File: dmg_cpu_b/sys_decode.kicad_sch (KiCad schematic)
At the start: 94 parts, among them T1 IBUF, T2 IBUF

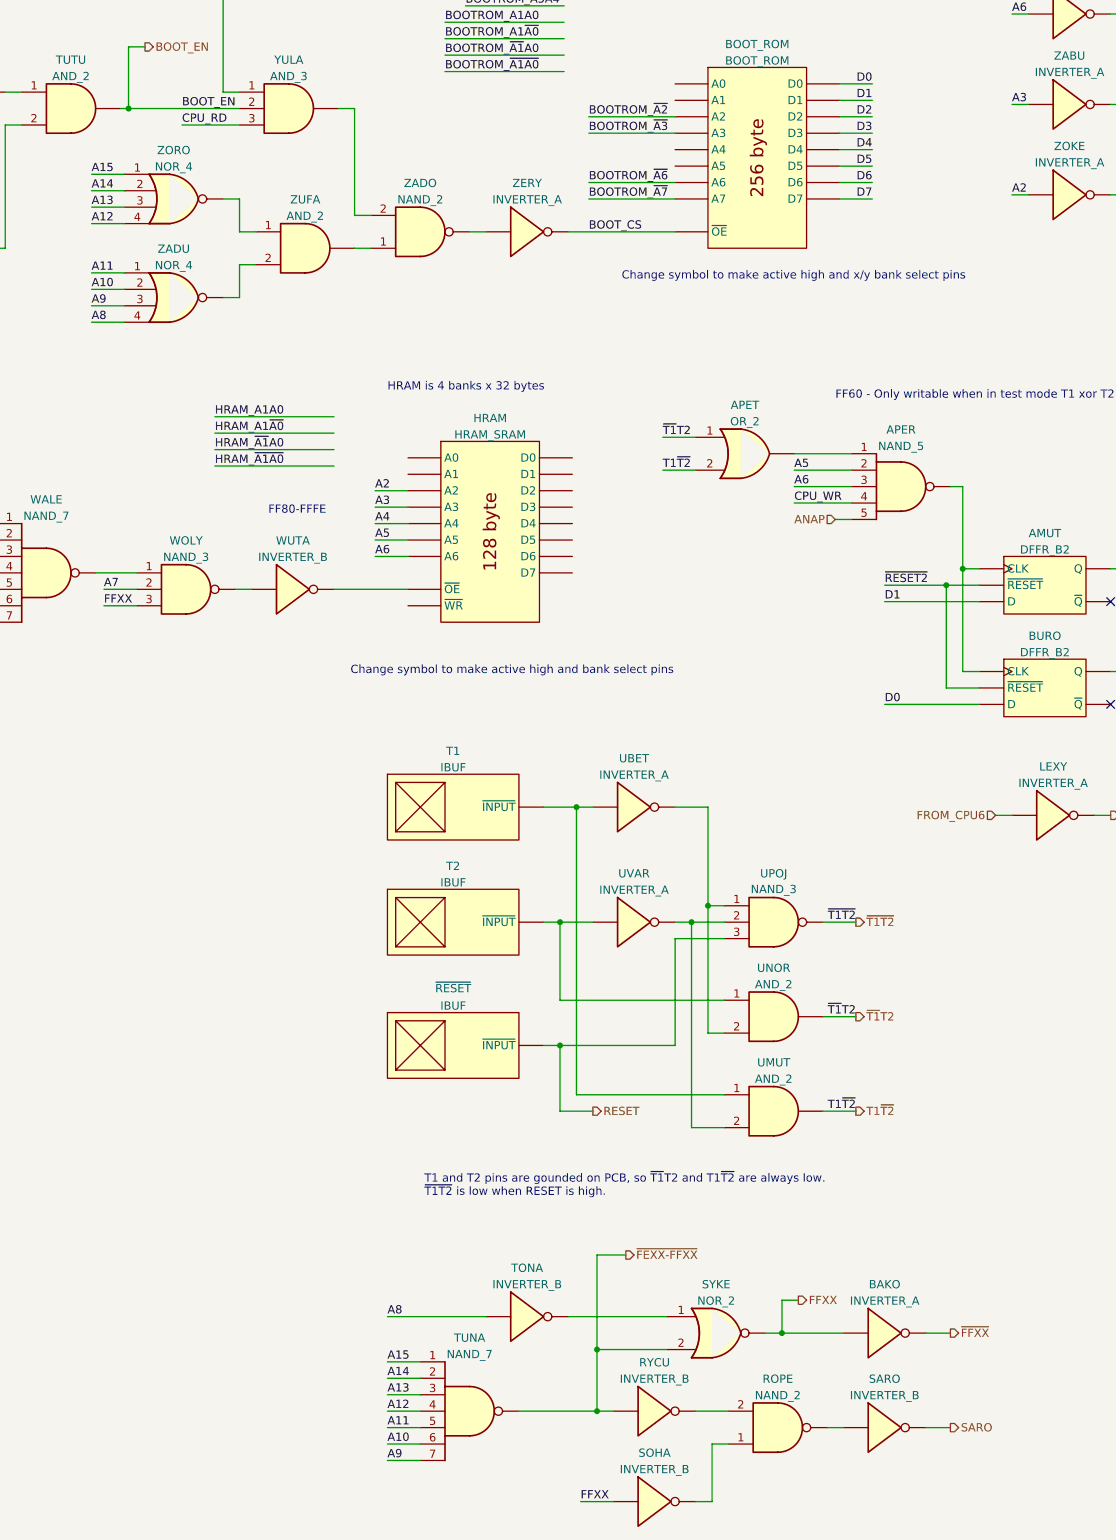
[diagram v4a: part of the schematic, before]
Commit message: Fixes made from issues, channel 4 sheet aded and tidy up of hierarchical APU sheet. Small fixes done here and there when doing ERC.
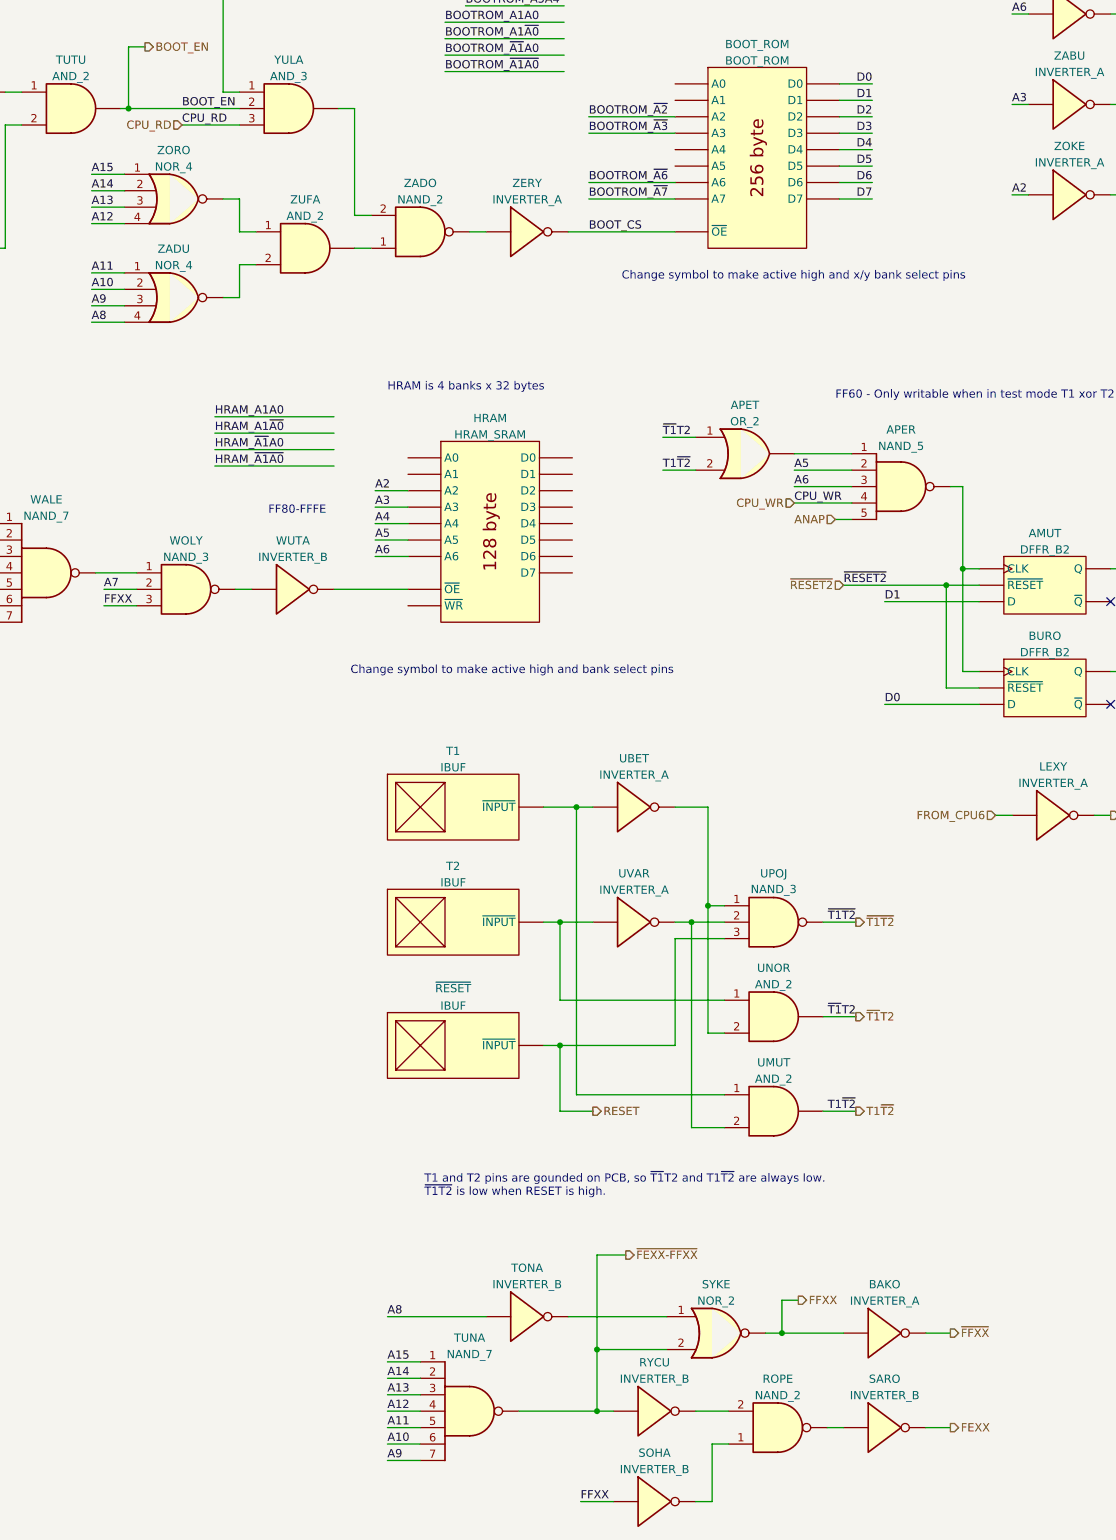
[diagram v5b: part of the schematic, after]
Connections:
- net SARO renamed FEXX
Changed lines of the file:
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@@
     (stroke (width 0) (type default) (color 0 0 0 0))
   )
-  (wire (pts (xy 271.145 132.08) (xy 280.67 132.08))
+  (wire (pts (xy 264.795 132.08) (xy 280.67 132.08))
     (stroke (width 0) (type default) (color 0 0 0 0))
   )
@@
     (effects (font (size 1.27 1.27)) (justify left bottom))
   )
-  (label "~{RESET2}" (at 271.145 132.08 0)
+  (label "~{RESET2}" (at 264.795 132.08 0)
     (effects (font (size 1.27 1.27)) (justify left bottom))
   )
@@
     (effects (font (size 1.27 1.27)) (justify left))
   )
+  (hierarchical_label "CPU_RD" (shape input) (at 162.56 60.96 180)
+    (effects (font (size 1.27 1.27)) (justify right))
+  )
+  (hierarchical_label "CPU_WR" (shape input) (at 257.175 119.38 180)
+    (effects (font (size 1.27 1.27)) (justify right))
+  )
   (hierarchical_label "FROM_CPU6" (shape input) (at 288.29 167.64 180)
     (effects (font (size 1.27 1.27)) (justify right))
@@
     (effects (font (size 1.27 1.27)) (justify left))
   )
+  (hierarchical_label "~{RESET2}" (shape input) (at 264.795 132.08 180)
+    (effects (font (size 1.27 1.27)) (justify right))
+  )
   (hierarchical_label "FF60_D0" (shape output) (at 308.61 145.415 0)
     (effects (font (size 1.27 1.27)) (justify left))
@@
     (effects (font (size 1.27 1.27)) (justify left))
   )
-  (hierarchical_label "SARO" (shape output) (at 281.305 262.255 0)
+  (hierarchical_label "FEXX" (shape output) (at 281.305 262.255 0)
     (effects (font (size 1.27 1.27)) (justify left))
   )
@@
   (symbol (lib_id "power:GND") (at 90.17 269.24 0) (unit 1)
     (in_bom yes) (on_board yes) (fields_autoplaced)
-    (property "Reference" "#PWR?" (id 0) (at 90.17 275.59 0)
+    (property "Reference" "#PWR0107" (id 0) (at 90.17 275.59 0)
       (effects (font (size 1.27 1.27)) hide)
     )
@@
   (symbol (lib_id "power:GND") (at 44.45 269.24 0) (unit 1)
     (in_bom yes) (on_board yes) (fields_autoplaced)
-    (property "Reference" "#PWR?" (id 0) (at 44.45 275.59 0)
-      (effects (font (size 1.27 1.27)) hide)
-    )
+    (property "Reference" "#PWR0104" (id 0) (at 44.45 275.59 0)
+      (effects (font (size 1.27 1.27)) hide)
+    )

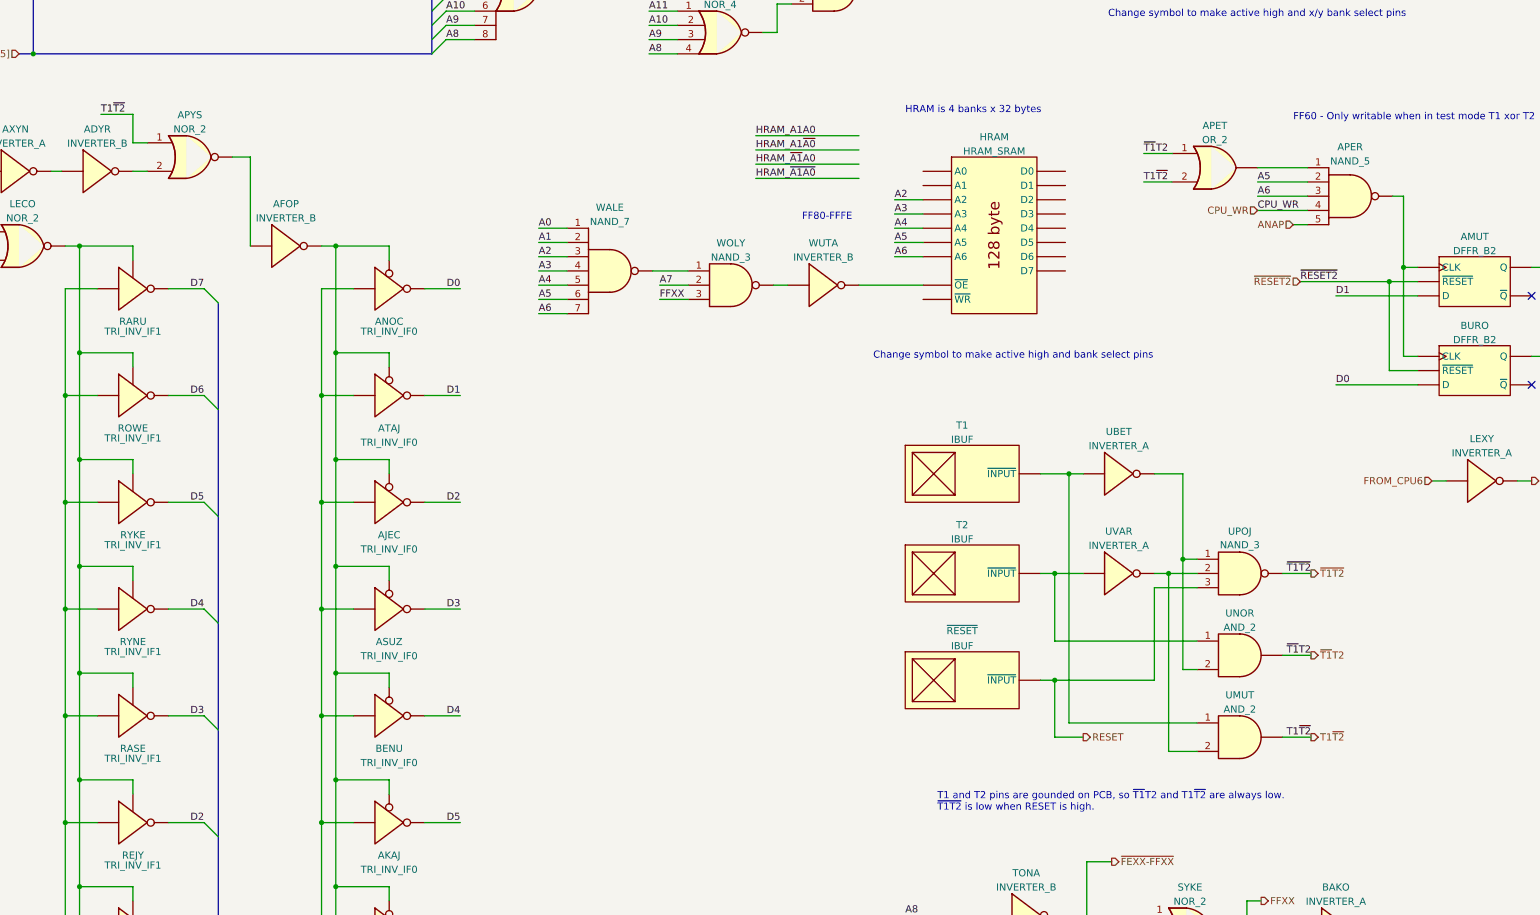
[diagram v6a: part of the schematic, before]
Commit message: Fixes made based on raised issues. PPU decode page added as draft level.
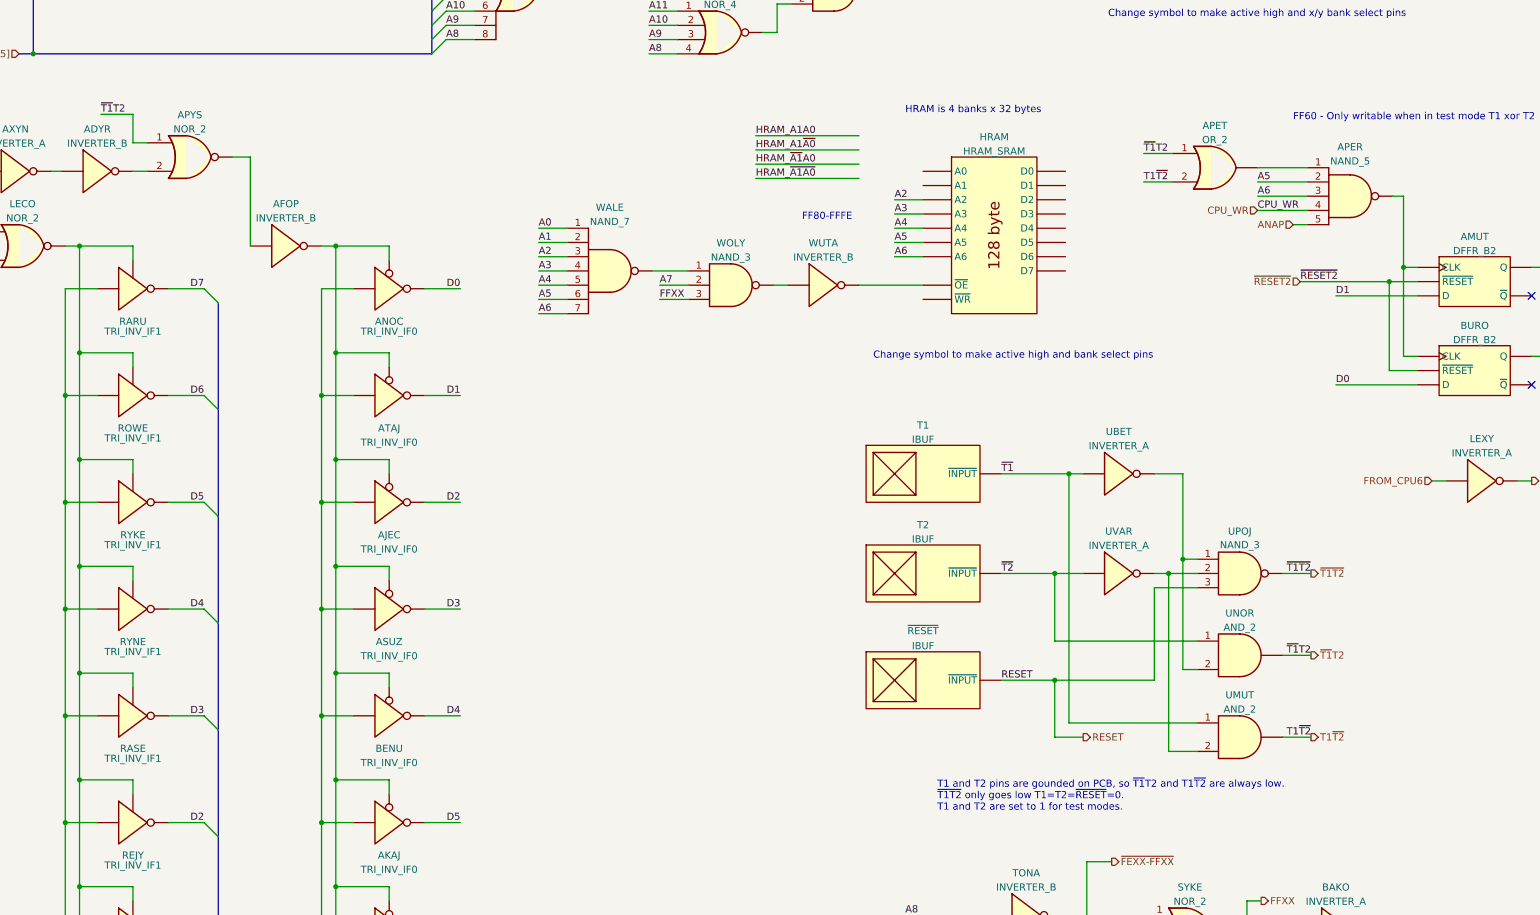
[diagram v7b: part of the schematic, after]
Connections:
- net T1~{T2}: no longer APYS.1
- net ~{T1}T2: now also APYS.1
- net ~{T1}: now reaches T1.1 (~{INPUT}), UBET.1, UMUT.1
- net ~{T2}: now reaches T2.1 (~{INPUT}), UNOR.1, UVAR.1
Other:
- note added: "T1 and T2 pins are gounded on PCB, so ~{T1}T2 and T1~{T2} are always low. ~{T1T2} only goes low T1=T2=~{RESET}=0. T1 and T2 are set to 1 for test modes."
- note removed: "T1 and T2 pins are gounded on PCB, so ~{T1}T2 and T1~{T2} are always low. ~{T1T2} is low when RESET is high."
- moved on the sheet: T1, T2, ~{RESET}
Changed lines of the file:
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@@
     (stroke (width 0) (type default) (color 0 0 0 0))
   )
-  (wire (pts (xy 220.98 203.2) (xy 218.44 203.2))
+  (wire (pts (xy 220.98 203.2) (xy 211.455 203.2))
     (stroke (width 0) (type default) (color 0 0 0 0))
   )
@@
     (stroke (width 0) (type default) (color 0 0 0 0))
   )
-  (wire (pts (xy 218.44 184.15) (xy 220.98 184.15))
+  (wire (pts (xy 211.455 184.15) (xy 220.98 184.15))
     (stroke (width 0) (type default) (color 0 0 0 0))
   )
@@
     (stroke (width 0) (type default) (color 0 0 0 0))
   )
-  (wire (pts (xy 218.44 166.37) (xy 223.52 166.37))
+  (wire (pts (xy 211.455 166.37) (xy 223.52 166.37))
     (stroke (width 0) (type default) (color 0 0 0 0))
   )
@@
     (effects (font (size 1.27 1.27)) (justify left bottom))
   )
-  (text "T1 and T2 pins are gounded on PCB, so ~{T1}T2 and T1~{T2} are always low.\n~{T1T2} is low when RESET is high."
+  (text "T1 and T2 pins are gounded on PCB, so ~{T1}T2 and T1~{T2} are always low.\n~{T1T2} only goes low T1=T2=~{RESET}=0.\nT1 and T2 are set to 1 for test modes."
     (at 200.025 226.695 0)
     (effects (font (size 1.27 1.27)) (justify left bottom))
@@
     (effects (font (size 1.27 1.27)) (justify left bottom))
   )
-  (label "T1~{T2}" (at 50.8 102.235 0)
-    (effects (font (size 1.27 1.27)) (justify left bottom))
-  )
   (label "BOOTROM_~{A1A0}" (at 405.765 158.115 180)
     (effects (font (size 1.27 1.27)) (justify right bottom))
@@
     (effects (font (size 1.27 1.27)) (justify left bottom))
   )
+  (label "~{T1}" (at 211.455 166.37 0)
+    (effects (font (size 1.27 1.27)) (justify left bottom))
+  )
   (label "A5" (at 41.275 45.085 0)
     (effects (font (size 1.27 1.27)) (justify left bottom))
@@
     (effects (font (size 1.27 1.27)) (justify right bottom))
   )
+  (label "~{T1}T2" (at 50.8 102.235 0)
+    (effects (font (size 1.27 1.27)) (justify left bottom))
+  )
   (label "A7" (at 290.83 29.845 0)
     (effects (font (size 1.27 1.27)) (justify left bottom))
@@
     (effects (font (size 1.27 1.27)) (justify left bottom))
   )
+  (label "~{T2}" (at 211.455 184.15 0)
+    (effects (font (size 1.27 1.27)) (justify left bottom))
+  )
   (label "A3" (at 290.83 57.785 0)
     (effects (font (size 1.27 1.27)) (justify left bottom))
@@
   )
   (label "FFXX" (at 60.325 53.975 0)
+    (effects (font (size 1.27 1.27)) (justify left bottom))
+  )
+  (label "RESET" (at 211.455 203.2 0)
     (effects (font (size 1.27 1.27)) (justify left bottom))
   )
@@
     (pin "2")
   )
-  (symbol (lib_id "DMG_CPU_Cells:IBUF") (at 204.47 166.37 0) (unit 1)
-    (in_bom yes) (on_board yes) (fields_autoplaced)
-    (property "Reference" "T1" (id 0) (at 204.47 157.7172 0))
-    (property "Value" "IBUF" (id 1) (at 204.47 160.2541 0))
-    (property "Footprint" "" (id 2) (at 204.47 166.37 0)
-      (effects (font (size 1.27 1.27)) hide)
-    )
-    (property "Datasheet" "http://iceboy.a-singer.de/doc/dmg_cells.html#ibuf" (id 3) (at 204.47 175.26 0)
+  (symbol (lib_id "DMG_CPU_Cells:IBUF") (at 197.485 166.37 0) (unit 1)
+    (in_bom yes) (on_board yes) (fields_autoplaced)
+    (property "Reference" "T1" (id 0) (at 197.485 157.7172 0))
+    (property "Value" "IBUF" (id 1) (at 197.485 160.2541 0))
+    (property "Footprint" "" (id 2) (at 197.485 166.37 0)
+      (effects (font (size 1.27 1.27)) hide)
+    )
+    (property "Datasheet" "http://iceboy.a-singer.de/doc/dmg_cells.html#ibuf" (id 3) (at 197.485 175.26 0)
       (effects (font (size 1.27 1.27)) hide)
     )
@@
     (pin "1")
   )
-  (symbol (lib_id "DMG_CPU_Cells:IBUF") (at 204.47 203.2 0) (unit 1)
-    (in_bom yes) (on_board yes) (fields_autoplaced)
-    (property "Reference" "~{RESET}" (id 0) (at 204.47 194.3932 0))
-    (property "Value" "IBUF" (id 1) (at 204.47 197.0841 0))
-    (property "Footprint" "" (id 2) (at 204.47 203.2 0)
-      (effects (font (size 1.27 1.27)) hide)
-    )
-    (property "Datasheet" "http://iceboy.a-singer.de/doc/dmg_cells.html#ibuf" (id 3) (at 204.47 212.09 0)
+  (symbol (lib_id "DMG_CPU_Cells:IBUF") (at 197.485 203.2 0) (unit 1)
+    (in_bom yes) (on_board yes) (fields_autoplaced)
+    (property "Reference" "~{RESET}" (id 0) (at 197.485 194.3932 0))
+    (property "Value" "IBUF" (id 1) (at 197.485 197.0841 0))
+    (property "Footprint" "" (id 2) (at 197.485 203.2 0)
+      (effects (font (size 1.27 1.27)) hide)
+    )
+    (property "Datasheet" "http://iceboy.a-singer.de/doc/dmg_cells.html#ibuf" (id 3) (at 197.485 212.09 0)
       (effects (font (size 1.27 1.27)) hide)
     )
@@
     (pin "2")
   )
-  (symbol (lib_id "DMG_CPU_Cells:IBUF") (at 204.47 184.15 0) (unit 1)
-    (in_bom yes) (on_board yes) (fields_autoplaced)
-    (property "Reference" "T2" (id 0) (at 204.47 175.4972 0))
-    (property "Value" "IBUF" (id 1) (at 204.47 178.0341 0))
-    (property "Footprint" "" (id 2) (at 204.47 184.15 0)
-      (effects (font (size 1.27 1.27)) hide)
-    )
-    (property "Datasheet" "http://iceboy.a-singer.de/doc/dmg_cells.html#ibuf" (id 3) (at 204.47 193.04 0)
-      (effects (font (size 1.27 1.27)) hide)
-    )
+  (symbol (lib_id "DMG_CPU_Cells:IBUF") (at 197.485 184.15 0) (unit 1)
+    (in_bom yes) (on_board yes) (fields_autoplaced)
+    (property "Reference" "T2" (id 0) (at 197.485 175.4972 0))
+    (property "Value" "IBUF" (id 1) (at 197.485 178.0341 0))
+    (property "Footprint" "" (id 2) (at 197.485 184.15 0)
+      (effects (font (size 1.27 1.27)) hide)
+    )
+    (property "Datasheet" "http://iceboy.a-singer.de/doc/dmg_cells.html#ibuf" (id 3) (at 197.485 193.04 0)
+      (effects (font (size 1.27 1.27)) hide)
+    )

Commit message: VRAM interface sheet added but various edits in existing sheets. Notable merge of RESET, CLOCKS and FF04 DIV sheets
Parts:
- removed AMUT, BURO: DFFR_B2, symbol DMG_CPU_Cells:DFFR_B2
- removed APER: NAND_5, symbol DMG_CPU_Cells:NAND_5
- removed APET: OR_2, symbol DMG_CPU_Cells:OR_2
- removed LEXY: INVERTER_A, symbol DMG_CPU_Cells:INVERTER_A
- added BAKO?, RUNY: INVERTER_A, symbol DMG_CPU_Cells:INVERTER_A
- added SEDU, SOSA, TAHY, TAXO, TAZU, TESU, TEWA, TOVU: TRI_BUF_IF0, symbol DMG_CPU_Cells:TRI_BUF_IF0
- added SOLE: INVERTER_B, symbol DMG_CPU_Cells:INVERTER_B
- added TUSO: NOR_2, symbol DMG_CPU_Cells:NOR_2
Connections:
- net D0: now also TAHY.4
- net D1: now also TESU.4
- net D2: now also TAXO.4
- net D3: now also TOVU.4
- net D4: now also TAZU.4
- net D5: now also TEWA.4
- net D6: now also SOSA.4
- net D7: now also SEDU.4
- net GND: now also RUNY.1, RUNY.2, SEDU.1 (IN), SEDU.3 (IN), SOSA.1 (IN), SOSA.3 (IN), TAHY.1 (IN), TAHY.3 (IN), TAXO.1 (IN), TAXO.3 (IN), TAZU.1 (IN), TAZU.3 (IN), TESU.1 (IN), TESU.3 (IN), TEWA.1 (IN), TEWA.3 (IN), TOVU.1 (IN), TOVU.3 (IN)
- net ~{FEXX-FFXX}: now also BAKO?.1
- net ~{T1}T2: now also TUSO.1
- net BEDO renamed DATA_VALID
- net DATA_VALID: now also TUSO.2
- new net: SEDU.2 (~{ENA}), SOLE.2, SOSA.2 (~{ENA}), TAHY.2 (~{ENA}), TAXO.2 (~{ENA}), TAZU.2 (~{ENA}), TESU.2 (~{ENA}), TEWA.2 (~{ENA}), TOVU.2 (~{ENA})
- new net: SOLE.1, TUSO.3
- new net FEXX-FFXX: BAKO?.2
- no-connect marks 2 -> 0
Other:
- note added: "Data bus is presented with 0xFF when BEDO is low; start of CPU cycle."
- note added: "FF50 BOOT EN"
- note removed: "FF50"
- note removed: "FF60 - Only writable when in test mode T1 xor T2"
- moved on the sheet: ADYR, AFOP, AJEC, AKAJ, ANOC, APYS, ARAR, ASUZ, ATAJ, AXYN, BAKO, BEDA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
